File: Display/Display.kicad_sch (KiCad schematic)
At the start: 9 parts, among them J1 Conn_01x60, J2 12402032E202A, J3 12402032E202A, J4 Conn_01x60

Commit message: save before 4 layers
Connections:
- net at S5.1: now also J4.2 (Pin_2); no longer J4.34 (Pin_34)
- net at S5.2: now also J4.3 (Pin_3); no longer J4.35 (Pin_35)
- net at S5.3: now also J4.4 (Pin_4); no longer J4.36 (Pin_36)
- net at S5.4: now also J4.6 (Pin_6); no longer J4.38 (Pin_38)
- net at S5.5: now also J4.7 (Pin_7); no longer J4.39 (Pin_39)
- net at S5.6: now also J4.8 (Pin_8); no longer J4.40 (Pin_40)
- net at S1.1: now also J4.34 (Pin_34); no longer J4.2 (Pin_2)
- net at S1.2: now also J4.35 (Pin_35); no longer J4.3 (Pin_3)
- net at S1.3: now also J4.36 (Pin_36); no longer J4.4 (Pin_4)
- net at S1.4: now also J4.38 (Pin_38); no longer J4.6 (Pin_6)
- net at S1.5: now also J4.39 (Pin_39); no longer J4.7 (Pin_7)
- net at S1.6: now also J4.40 (Pin_40); no longer J4.8 (Pin_8)
- net at S2.1: now also J4.26 (Pin_26); no longer J4.10 (Pin_10)
- net at S2.2: now also J4.27 (Pin_27); no longer J4.11 (Pin_11)
- net at S2.3: now also J4.28 (Pin_28); no longer J4.12 (Pin_12)
- net at S2.4: now also J4.30 (Pin_30); no longer J4.14 (Pin_14)
- net at S2.5: now also J4.31 (Pin_31); no longer J4.15 (Pin_15)
- net at S2.6: now also J4.32 (Pin_32); no longer J4.16 (Pin_16)
- net at S4.1: now also J4.10 (Pin_10); no longer J4.26 (Pin_26)
- net at S4.2: now also J4.11 (Pin_11); no longer J4.27 (Pin_27)
- net at S4.3: now also J4.12 (Pin_12); no longer J4.28 (Pin_28)
- net at S4.4: now also J4.14 (Pin_14); no longer J4.30 (Pin_30)
- net at S4.5: now also J4.15 (Pin_15); no longer J4.31 (Pin_31)
- net at S4.6: now also J4.16 (Pin_16); no longer J4.32 (Pin_32)
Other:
- moved on the sheet: S1, S2, S4, S5

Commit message: user save
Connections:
- net GNDD: now also J4.46 (Pin_46), J4.47 (Pin_47), J4.48 (Pin_48), J4.49 (Pin_49), J4.50 (Pin_50), J4.51 (Pin_51); no longer J4.1 (Pin_1), J4.13 (Pin_13), J4.17 (Pin_17), J4.21 (Pin_21), J4.25 (Pin_25), J4.29 (Pin_29), J4.33 (Pin_33), J4.37 (Pin_37), J4.41 (Pin_41), J4.5 (Pin_5), J4.9 (Pin_9)
- net VCC: now also J4.30 (Pin_30), J4.31 (Pin_31), J4.32 (Pin_32), J4.33 (Pin_33), J4.34 (Pin_34), J4.35 (Pin_35), J4.36 (Pin_36), J4.37 (Pin_37), J4.38 (Pin_38), J4.39 (Pin_39), J4.40 (Pin_40), J4.41 (Pin_41); no longer J4.46 (Pin_46), J4.47 (Pin_47), J4.48 (Pin_48), J4.49 (Pin_49), J4.50 (Pin_50), J4.51 (Pin_51)
- net at S5.1: now also J4.28 (Pin_28); no longer J4.2 (Pin_2)
- net at S5.2: now also J4.26 (Pin_26); no longer J4.3 (Pin_3)
- net at S5.3: now also J4.24 (Pin_24); no longer J4.4 (Pin_4)
- net at S5.4: now also J4.29 (Pin_29); no longer J4.6 (Pin_6)
- net at S5.5: now also J4.27 (Pin_27); no longer J4.7 (Pin_7)
- net at S5.6: now also J4.25 (Pin_25); no longer J4.8 (Pin_8)
- net at S3.1: now also J4.11 (Pin_11); no longer J4.18 (Pin_18)
- net at S3.2: now also J4.9 (Pin_9); no longer J4.19 (Pin_19)
- net at S3.3: now also J4.7 (Pin_7); no longer J4.20 (Pin_20)
- net at S3.4: now also J4.12 (Pin_12); no longer J4.22 (Pin_22)
- net at S3.5: now also J4.10 (Pin_10); no longer J4.23 (Pin_23)
- net at S3.6: now also J4.8 (Pin_8); no longer J4.24 (Pin_24)
- net at S1.1: now also J4.13 (Pin_13); no longer J4.34 (Pin_34)
- net at S1.2: now also J4.15 (Pin_15); no longer J4.35 (Pin_35)
- net at S1.3: no longer J4.36 (Pin_36)
- net at S1.4: now also J4.14 (Pin_14); no longer J4.38 (Pin_38)
- net at S1.5: now also J4.16 (Pin_16); no longer J4.39 (Pin_39)
- net at S1.6: now also J4.17 (Pin_17); no longer J4.40 (Pin_40)
- net at S2.1: now also J4.1 (Pin_1); no longer J4.26 (Pin_26)
- net at S2.2: now also J4.3 (Pin_3); no longer J4.27 (Pin_27)
- net at S2.3: now also J4.5 (Pin_5); no longer J4.28 (Pin_28)
- net at S2.4: now also J4.2 (Pin_2); no longer J4.30 (Pin_30)
- net at S2.5: now also J4.4 (Pin_4); no longer J4.31 (Pin_31)
- net at S2.6: now also J4.6 (Pin_6); no longer J4.32 (Pin_32)
- net at S4.1: now also J4.22 (Pin_22); no longer J4.10 (Pin_10)
- net at S4.2: now also J4.20 (Pin_20); no longer J4.11 (Pin_11)
- net at S4.3: now also J4.18 (Pin_18); no longer J4.12 (Pin_12)
- net at S4.4: now also J4.23 (Pin_23); no longer J4.14 (Pin_14)
- net at S4.5: now also J4.21 (Pin_21); no longer J4.15 (Pin_15)
- net at S4.6: now also J4.19 (Pin_19); no longer J4.16 (Pin_16)
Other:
- moved on the sheet: J4, S1, S2, S3, S4, S5

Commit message: route buttons
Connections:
- net VCC: no longer J4.30 (Pin_30)
- net at S5.1: now also J4.29 (Pin_29); no longer J4.28 (Pin_28)
- net at S5.2: now also J4.27 (Pin_27); no longer J4.26 (Pin_26)
- net at S5.3: now also J4.25 (Pin_25); no longer J4.24 (Pin_24)
- net at S5.4: now also J4.30 (Pin_30); no longer J4.29 (Pin_29)
- net at S5.5: now also J4.28 (Pin_28); no longer J4.27 (Pin_27)
- net at S5.6: now also J4.26 (Pin_26); no longer J4.25 (Pin_25)
- net at S1.3: now also J4.17 (Pin_17)
- net at S1.6: now also J4.18 (Pin_18); no longer J4.17 (Pin_17)
- net at S4.1: now also J4.23 (Pin_23); no longer J4.22 (Pin_22)
- net at S4.2: now also J4.21 (Pin_21); no longer J4.20 (Pin_20)
- net at S4.3: now also J4.19 (Pin_19); no longer J4.18 (Pin_18)
- net at S4.4: now also J4.24 (Pin_24); no longer J4.23 (Pin_23)
- net at S4.5: now also J4.22 (Pin_22); no longer J4.21 (Pin_21)
- net at S4.6: now also J4.20 (Pin_20); no longer J4.19 (Pin_19)
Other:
- moved on the sheet: S4, S5

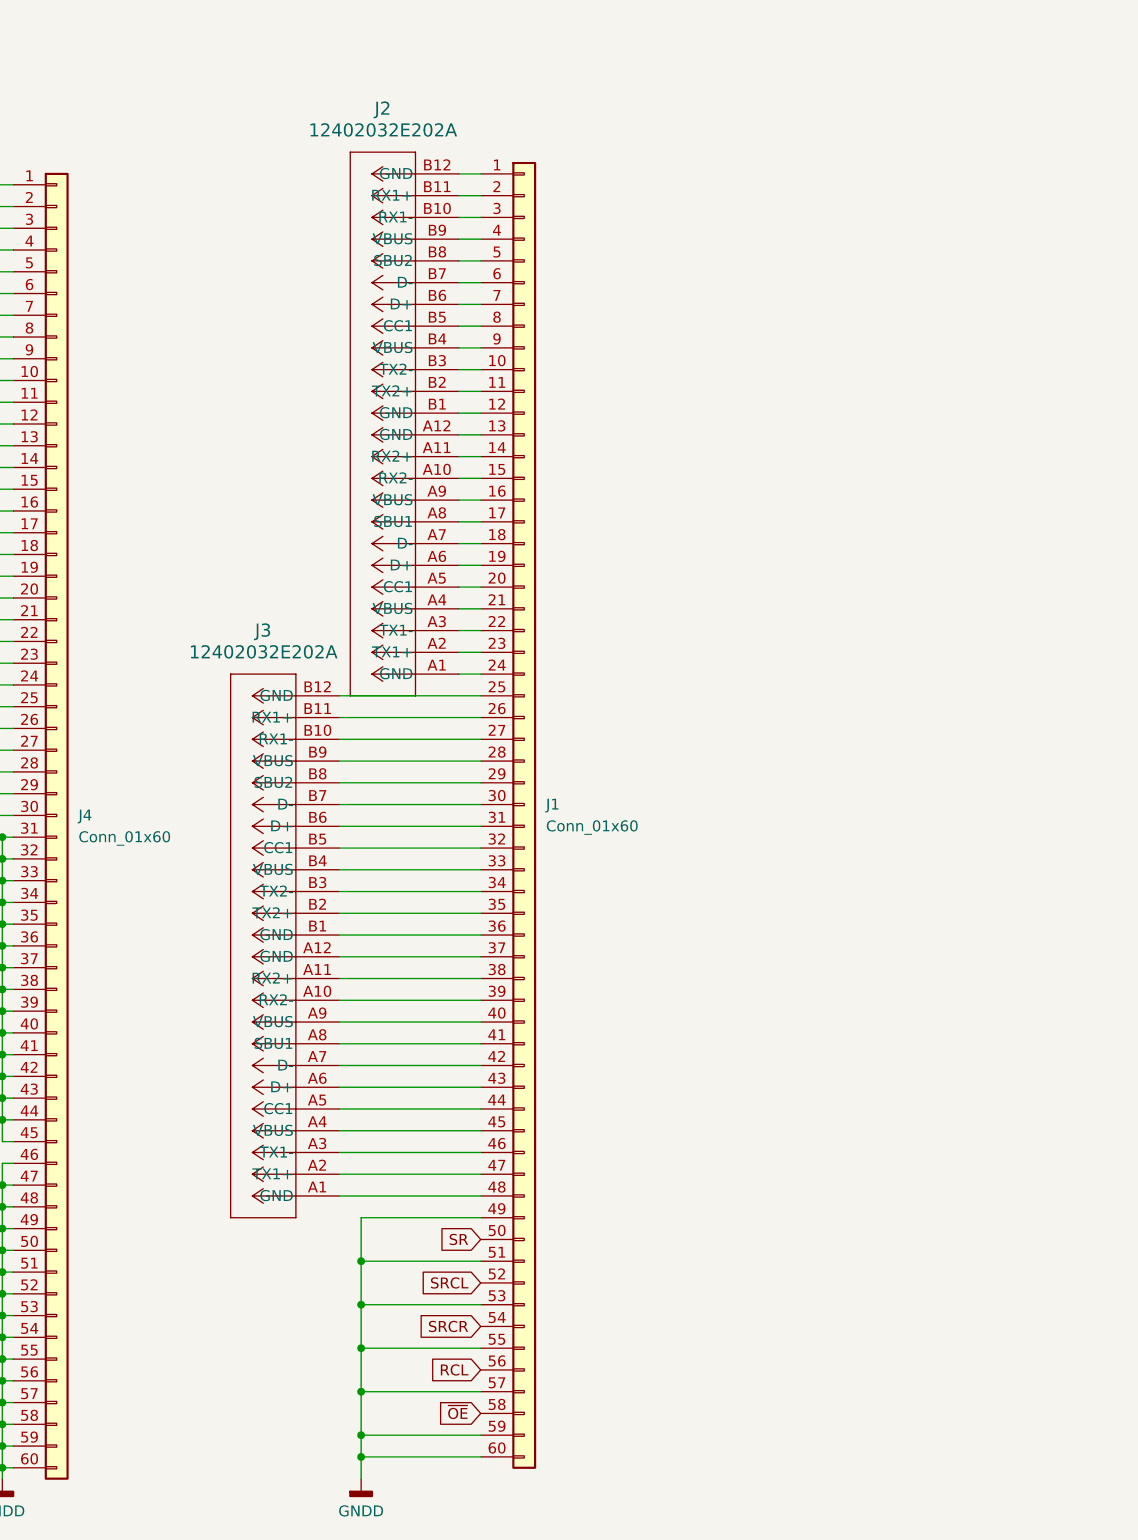
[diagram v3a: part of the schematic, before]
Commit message: optimize usb lanes
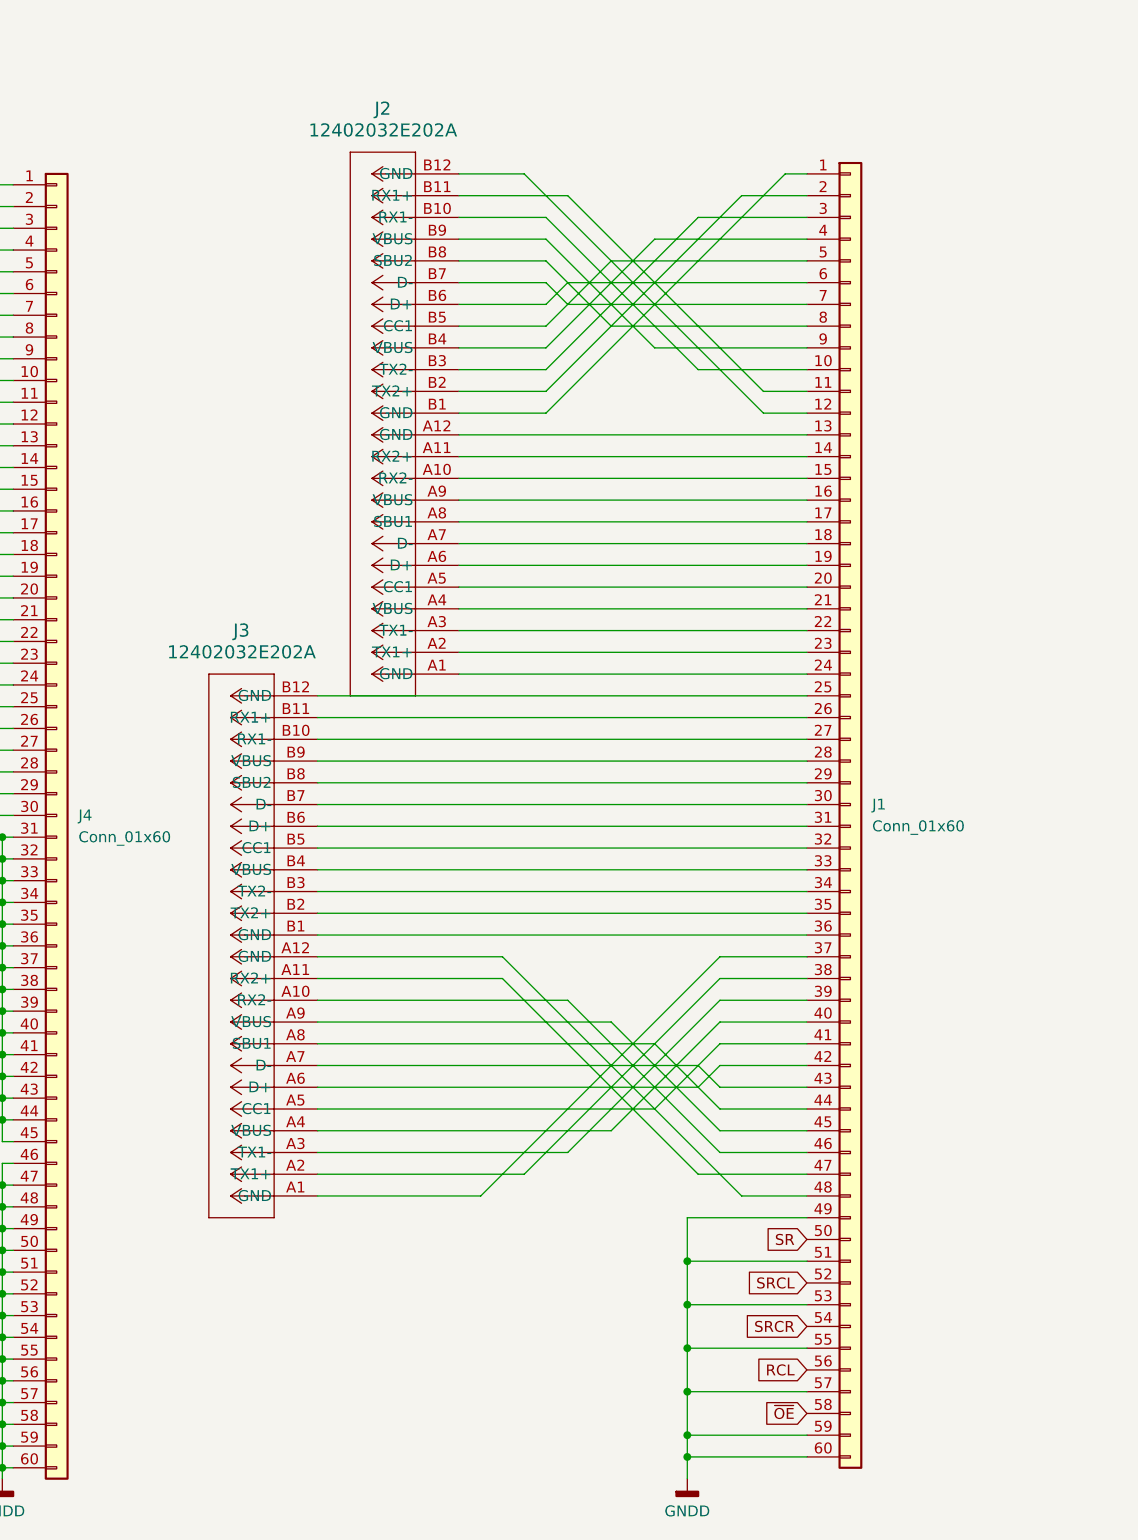
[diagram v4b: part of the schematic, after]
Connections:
- net at J2.B1 (GND): now also J1.1 (Pin_1); no longer J1.12 (Pin_12)
- net at J2.B10 (RX1-): now also J1.10 (Pin_10); no longer J1.3 (Pin_3)
- net at J2.B11 (RX1+): now also J1.11 (Pin_11); no longer J1.2 (Pin_2)
- net at J2.B12 (GND): now also J1.12 (Pin_12); no longer J1.1 (Pin_1)
- net at J2.B2 (TX2+): now also J1.2 (Pin_2); no longer J1.11 (Pin_11)
- net at J2.B3 (TX2-): now also J1.3 (Pin_3); no longer J1.10 (Pin_10)
- net at J2.B4 (VBUS): now also J1.4 (Pin_4); no longer J1.9 (Pin_9)
- net at J2.B5 (CC1): now also J1.5 (Pin_5); no longer J1.8 (Pin_8)
- net at J2.B6 (D+): now also J1.6 (Pin_6); no longer J1.7 (Pin_7)
- net at J2.B7 (D-): now also J1.7 (Pin_7); no longer J1.6 (Pin_6)
- net at J2.B8 (SBU2): now also J1.8 (Pin_8); no longer J1.5 (Pin_5)
- net at J2.B9 (VBUS): now also J1.9 (Pin_9); no longer J1.4 (Pin_4)
- net at J1.37 (Pin_37): now also J3.A1 (GND); no longer J3.A12 (GND)
- net at J1.38 (Pin_38): now also J3.A2 (TX1+); no longer J3.A11 (RX2+)
- net at J1.39 (Pin_39): now also J3.A3 (TX1-); no longer J3.A10 (RX2-)
- net at J1.40 (Pin_40): now also J3.A4 (VBUS); no longer J3.A9 (VBUS)
- net at J1.41 (Pin_41): now also J3.A5 (CC1); no longer J3.A8 (SBU1)
- net at J1.42 (Pin_42): now also J3.A6 (D+); no longer J3.A7 (D-)
- net at J1.43 (Pin_43): now also J3.A7 (D-); no longer J3.A6 (D+)
- net at J1.44 (Pin_44): now also J3.A8 (SBU1); no longer J3.A5 (CC1)
- net at J1.45 (Pin_45): now also J3.A9 (VBUS); no longer J3.A4 (VBUS)
- net at J1.46 (Pin_46): now also J3.A10 (RX2-); no longer J3.A3 (TX1-)
- net at J1.47 (Pin_47): now also J3.A11 (RX2+); no longer J3.A2 (TX1+)
- net at J1.48 (Pin_48): now also J3.A12 (GND); no longer J3.A1 (GND)
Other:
- moved on the sheet: J1, J3
